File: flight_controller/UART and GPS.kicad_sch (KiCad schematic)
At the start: 18 parts, among them CN1 A1257WV-S-6P, CN4 A1257WV-S-6P, CN5 A1257WV-S-6P

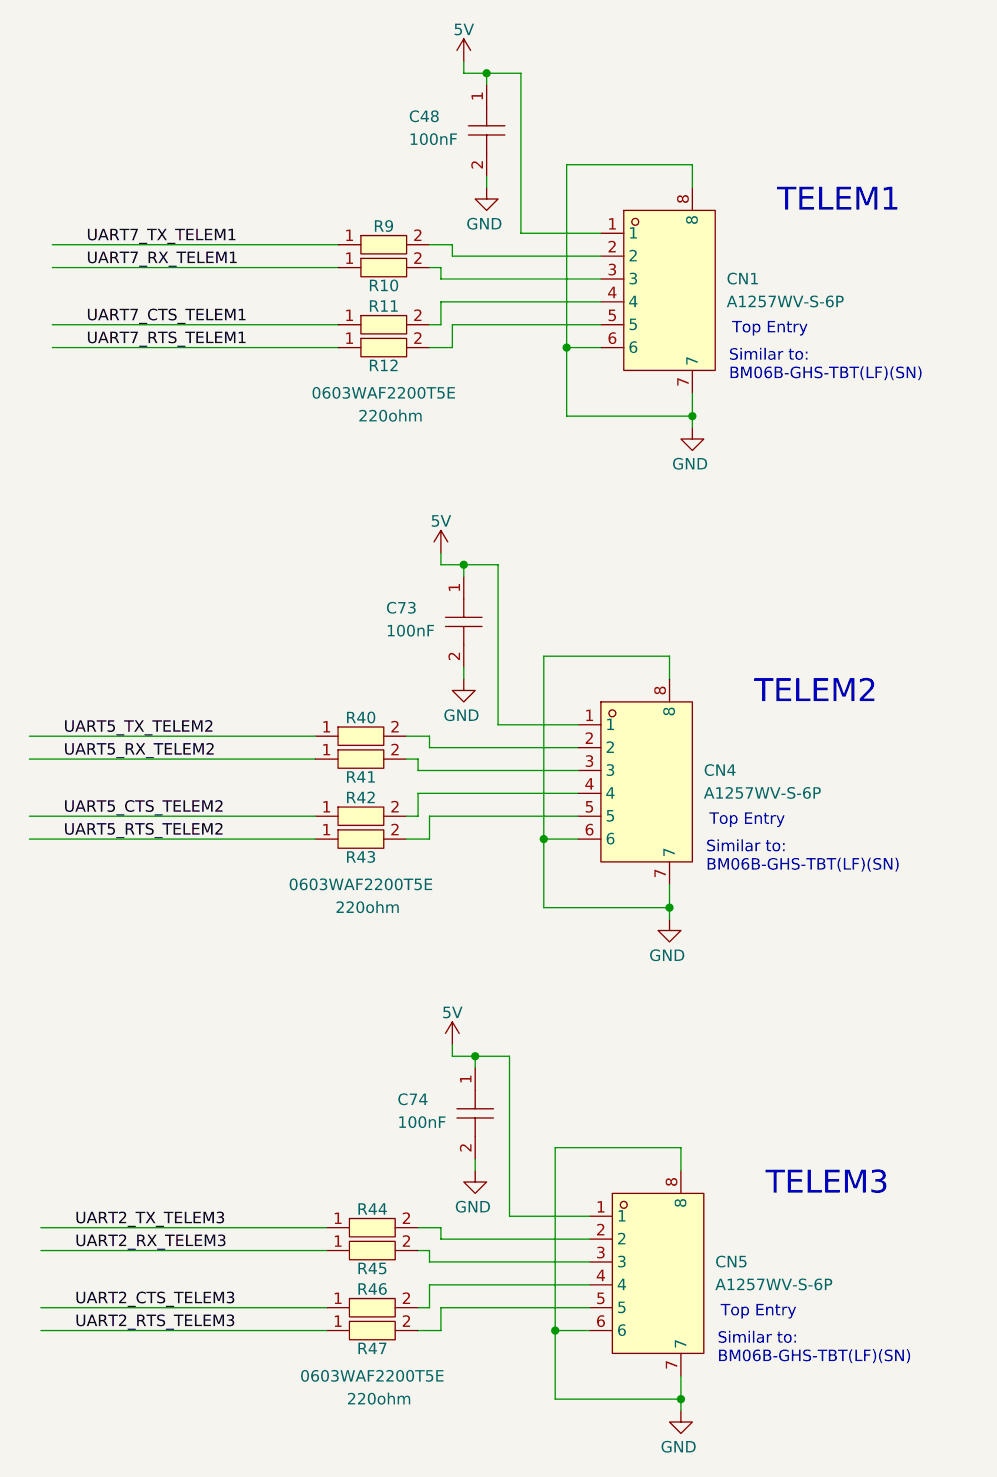
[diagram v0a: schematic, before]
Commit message: updating symbols as in the shared library
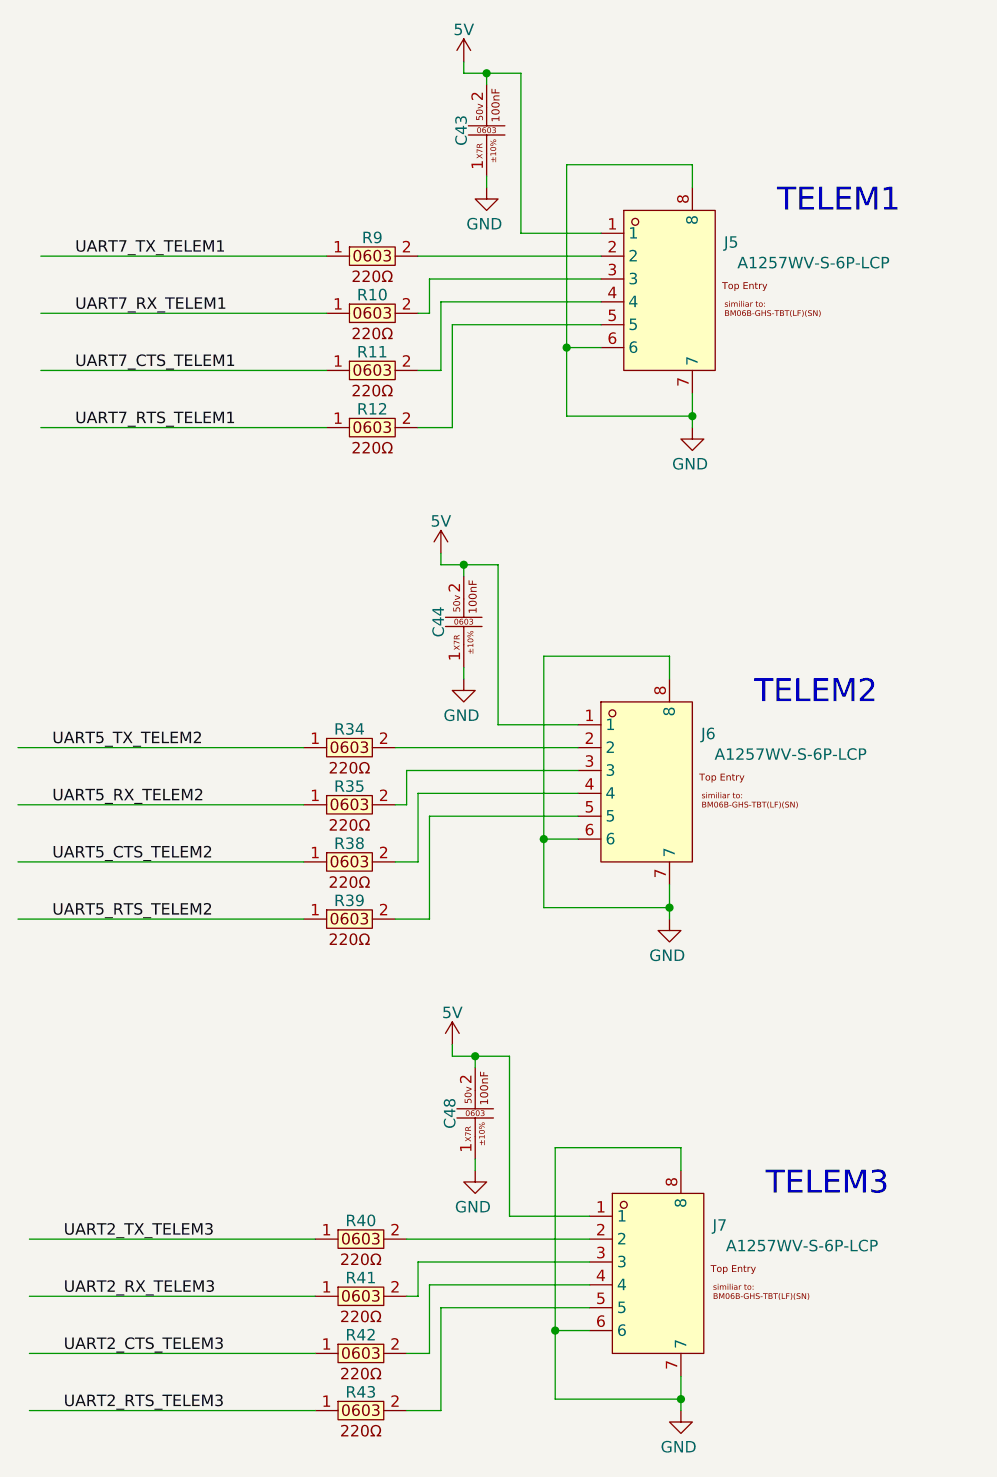
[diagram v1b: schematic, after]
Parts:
- removed C48, C73, C74: CC0402JRX7R7BB104, easyeda2kicad:C0402, symbol easyeda2kicad:CC0402JRX7R7BB104
- removed CN1, CN4, CN5: A1257WV-S-6P, easyeda2kicad:CONN-SMD_A1257WV-S-6P, symbol lampelKicadLIB:A1257WV-S-6P
- removed R10, R11, R12, R40, R41, R42, R43, R44, R45, R46, R47, R9: 0603WAF2200T5E, easyeda2kicad:R0603, symbol lampelKicadLIB:0603WAF2200T5E
- added C43, C44, C48: CC0603KRX7R9BB104 (100nf , 0603 ,50v ,X7R), easyeda2kicad:C0603, symbol lampelKicadLIB:CC0603KRX7R9BB104 (100nf , 0603 ,50v ,X7R)
- added J5, J6, J7: A1257WV-S-6P-LCP, easyeda2kicad:CONN-SMD_A1257WV-S-6P, symbol lampelKicadLIB:A1257WV-S-6P-LCP
- added R10, R11, R12, R34, R35, R38, R39, R40, R41, R42, R43, R9: 0603WAF2200T5E (220ohm , 0603), easyeda2kicad:R0603, symbol lampelKicadLIB:0603WAF2200T5E (220ohm , 0603)
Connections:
- net 5V: now also C43.2, C44.2, C48.2, J5.1, J6.1, J7.1
- net GND: now also C43.1, C44.1, C48.1, J5.6, J5.7, J5.8, J6.6, J6.7, J6.8, J7.6, J7.7, J7.8
- net UART2_CTS_TELEM3: now also R42.1
- net UART2_RTS_TELEM3: now also R43.1
- net UART2_RX_TELEM3: now also R41.1
- net UART2_TX_TELEM3: now also R40.1
- net UART5_CTS_TELEM2: now also R38.1
- net UART5_RTS_TELEM2: now also R39.1
- net UART5_RX_TELEM2: now also R35.1
- net UART5_TX_TELEM2: now also R34.1
- net UART7_CTS_TELEM1: now also R11.1
- net UART7_RTS_TELEM1: now also R12.1
- net UART7_RX_TELEM1: now also R10.1
- net UART7_TX_TELEM1: now also R9.1
- new net: J7.4, R42.2
- new net: J7.5, R43.2
- new net: J6.4, R38.2
- new net: J7.2, R40.2
- new net: J6.2, R34.2
- new net: J6.3, R35.2
- new net: J6.5, R39.2
- new net: J5.2, R9.2
- new net: J5.3, R10.2
- new net: J5.4, R11.2
- new net: J5.5, R12.2
- new net: J7.3, R41.2
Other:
- note removed: "Similar to: BM06B-GHS-TBT(LF)(SN)"
- note removed: "Top Entry"

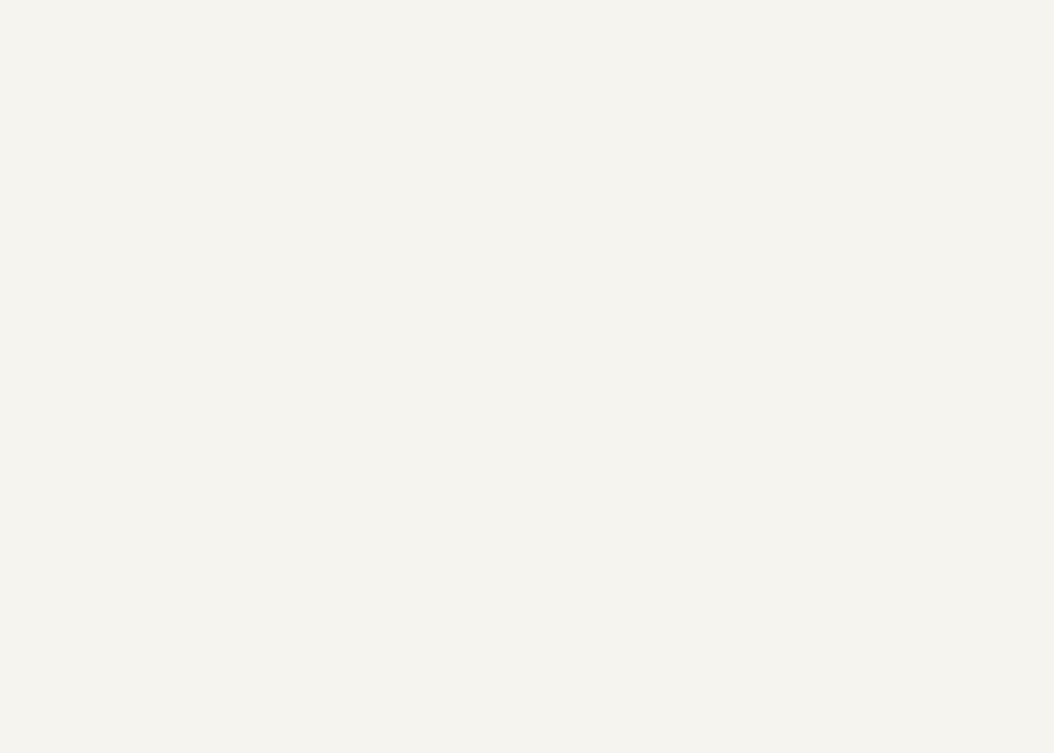
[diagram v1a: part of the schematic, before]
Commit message: update debug conn
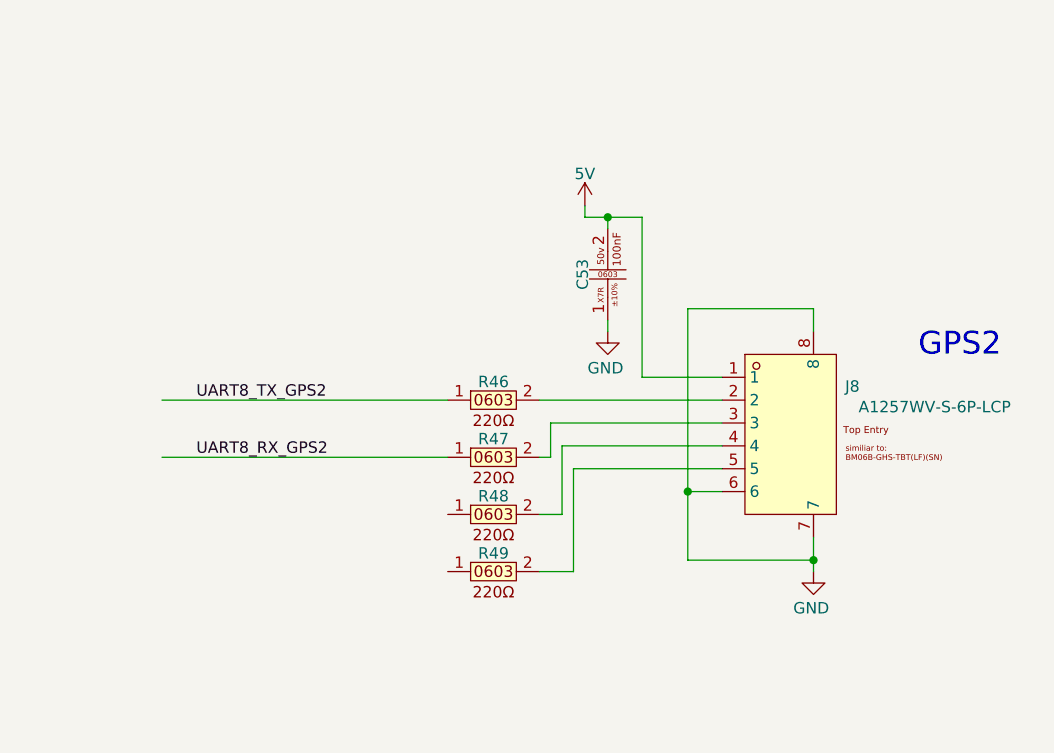
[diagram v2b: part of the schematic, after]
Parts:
- added C53: CC0603KRX7R9BB104 (100nf , 0603 ,50v ,X7R), easyeda2kicad:C0603, symbol lampelKicadLIB:CC0603KRX7R9BB104 (100nf , 0603 ,50v ,X7R)
- added J8: A1257WV-S-6P-LCP, easyeda2kicad:CONN-SMD_A1257WV-S-6P, symbol lampelKicadLIB:A1257WV-S-6P-LCP
- added R46, R47, R48, R49: 0603WAF2200T5E (220ohm , 0603), easyeda2kicad:R0603, symbol lampelKicadLIB:0603WAF2200T5E (220ohm , 0603)
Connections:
- net 5V: now also C53.2, J8.1
- net GND: now also C53.1, J8.6, J8.7, J8.8
- new net: J8.5, R49.2
- new net: J8.2, R46.2
- new net: J8.4, R48.2
- new net: J8.3, R47.2
- new net UART8_RX_GPS2: R47.1
- new net UART8_TX_GPS2: R46.1
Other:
- note added: "GPS2"

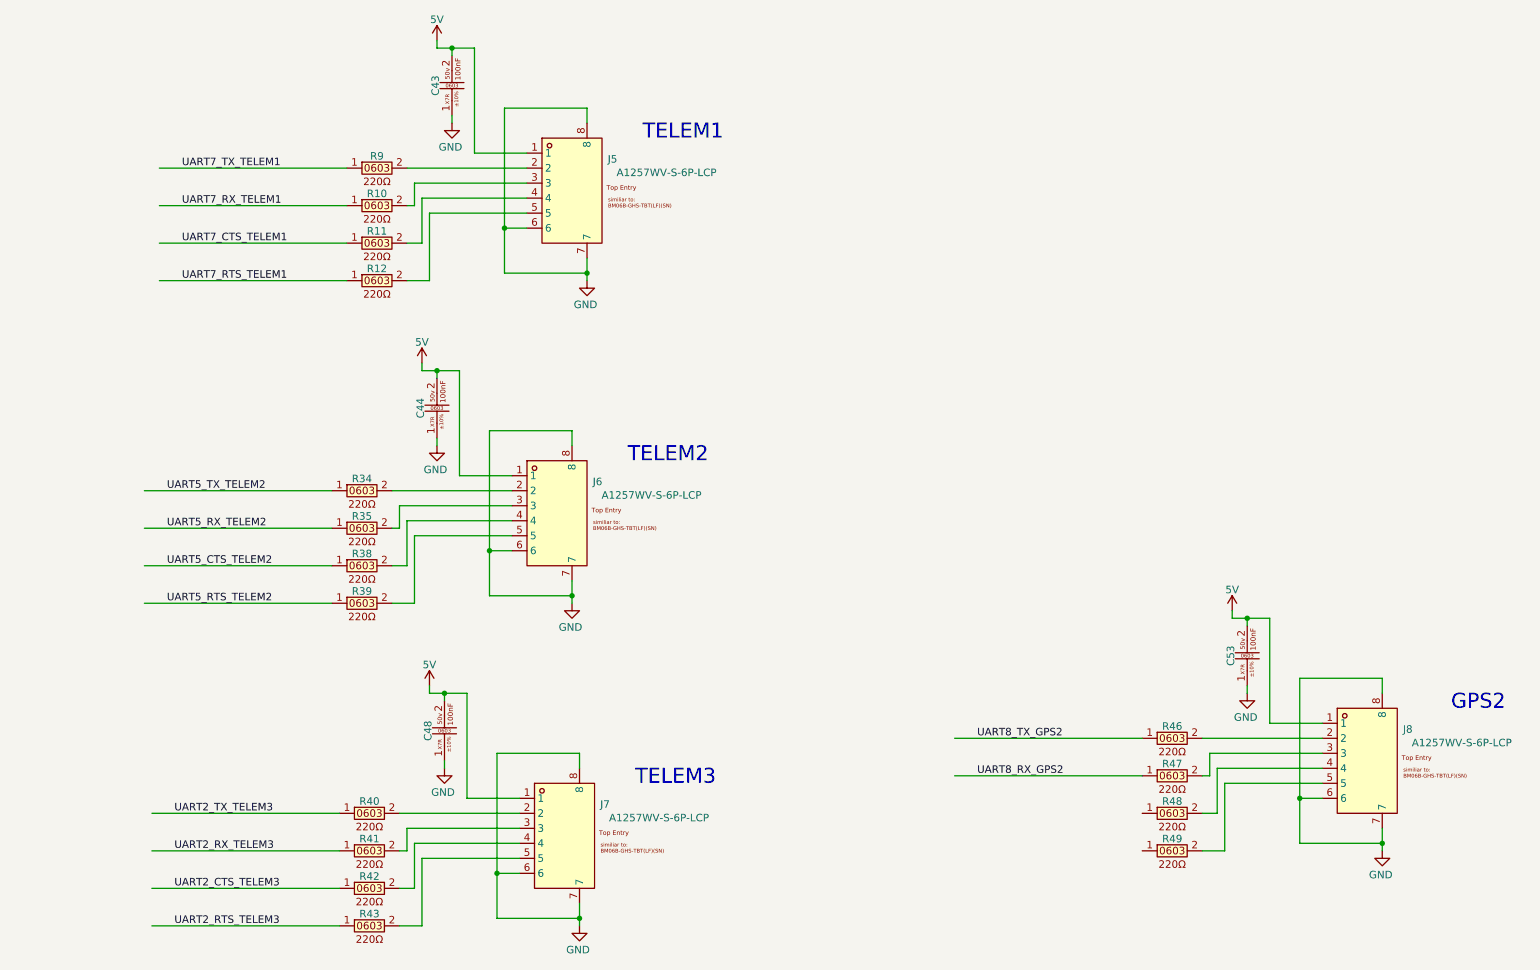
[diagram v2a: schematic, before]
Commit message: gps and power blocks
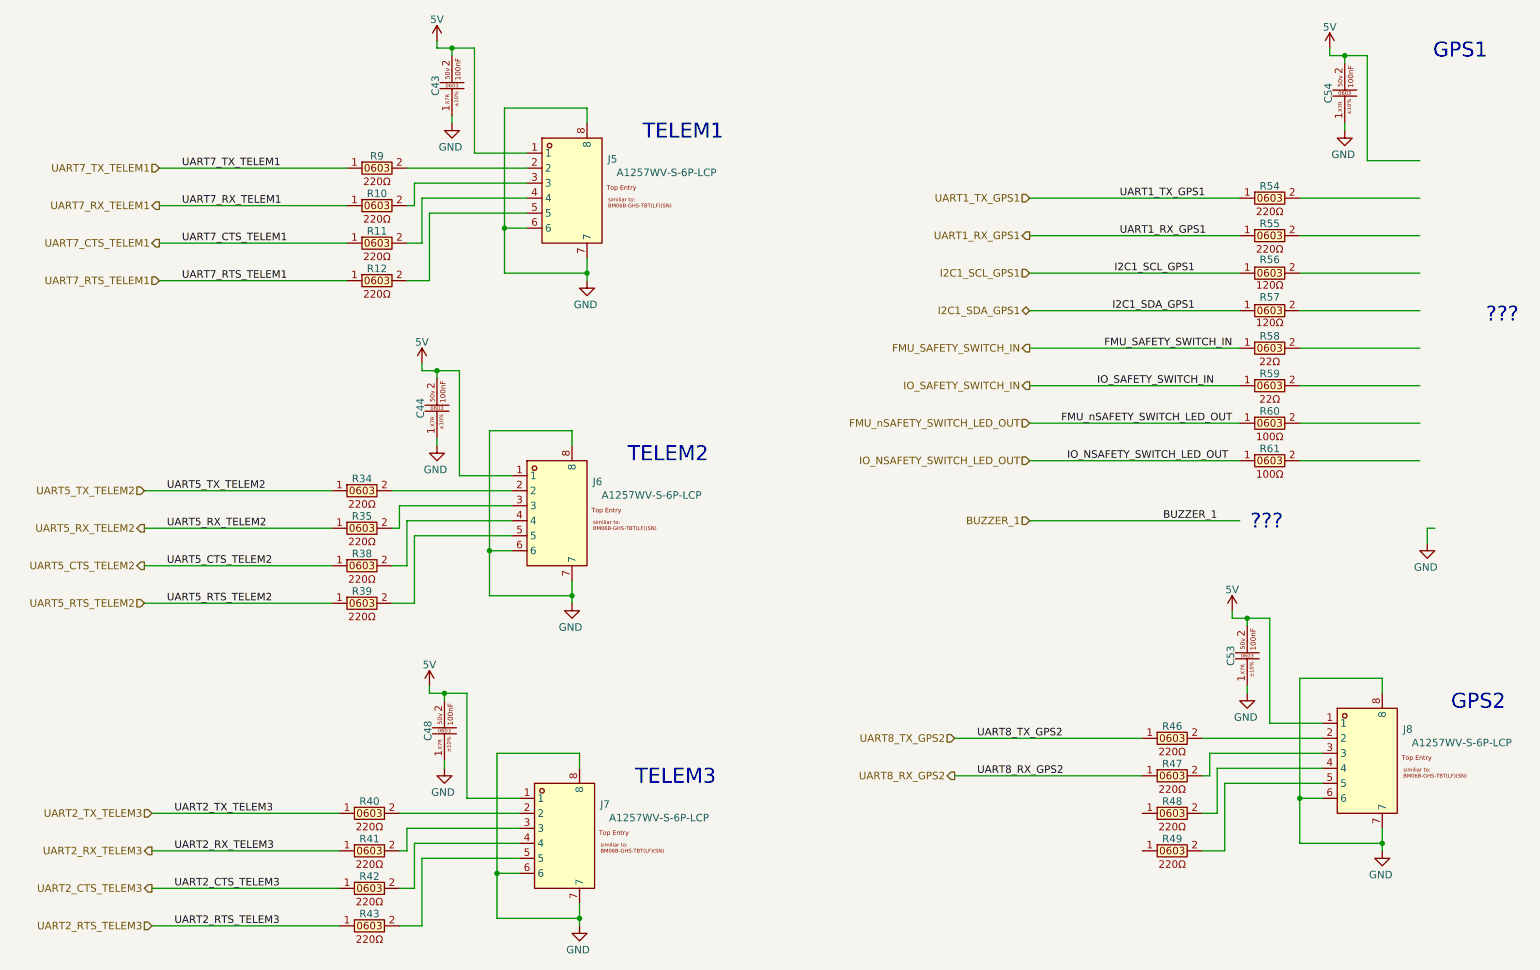
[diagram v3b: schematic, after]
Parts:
- added C54: CC0603KRX7R9BB104 (100nf , 0603 ,50v ,X7R), easyeda2kicad:C0603, symbol lampelKicadLIB:CC0603KRX7R9BB104 (100nf , 0603 ,50v ,X7R)
- added R54, R55: 0603WAF2200T5E (220ohm , 0603), easyeda2kicad:R0603, symbol lampelKicadLIB:0603WAF2200T5E (220ohm , 0603)
- added R56, R57: 603WAF1200T5E, easyeda2kicad:R0603, symbol lampelKicadLIB:0603WAF1200T5E (120ohm,0603)
- added R58, R59: 603WAF220JT5E (22ohm , 0603), easyeda2kicad:R0603, symbol lampelKicadLIB:0603WAF220JT5E (22ohm , 0603)
- added R60, R61: 603WAF1000T5E (100ohm , 0603), easyeda2kicad:R0603, symbol lampelKicadLIB:0603WAF1000T5E (100ohm , 0603)
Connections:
- net 5V: now also C54.2
- net GND: now also C54.1
- new net FMU_SAFETY_SWITCH_IN: R58.1
- new net FMU_nSAFETY_SWITCH_LED_OUT: R60.1
- new net I2C1_SCL_GPS1: R56.1
- new net I2C1_SDA_GPS1: R57.1
- new net IO_NSAFETY_SWITCH_LED_OUT: R61.1
- new net IO_SAFETY_SWITCH_IN: R59.1
- new net UART1_RX_GPS1: R55.1
- new net UART1_TX_GPS1: R54.1
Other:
- note added: "???"
- note added: "GPS1"
